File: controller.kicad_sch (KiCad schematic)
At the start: 23 parts, among them U4 STM32H742VGTx

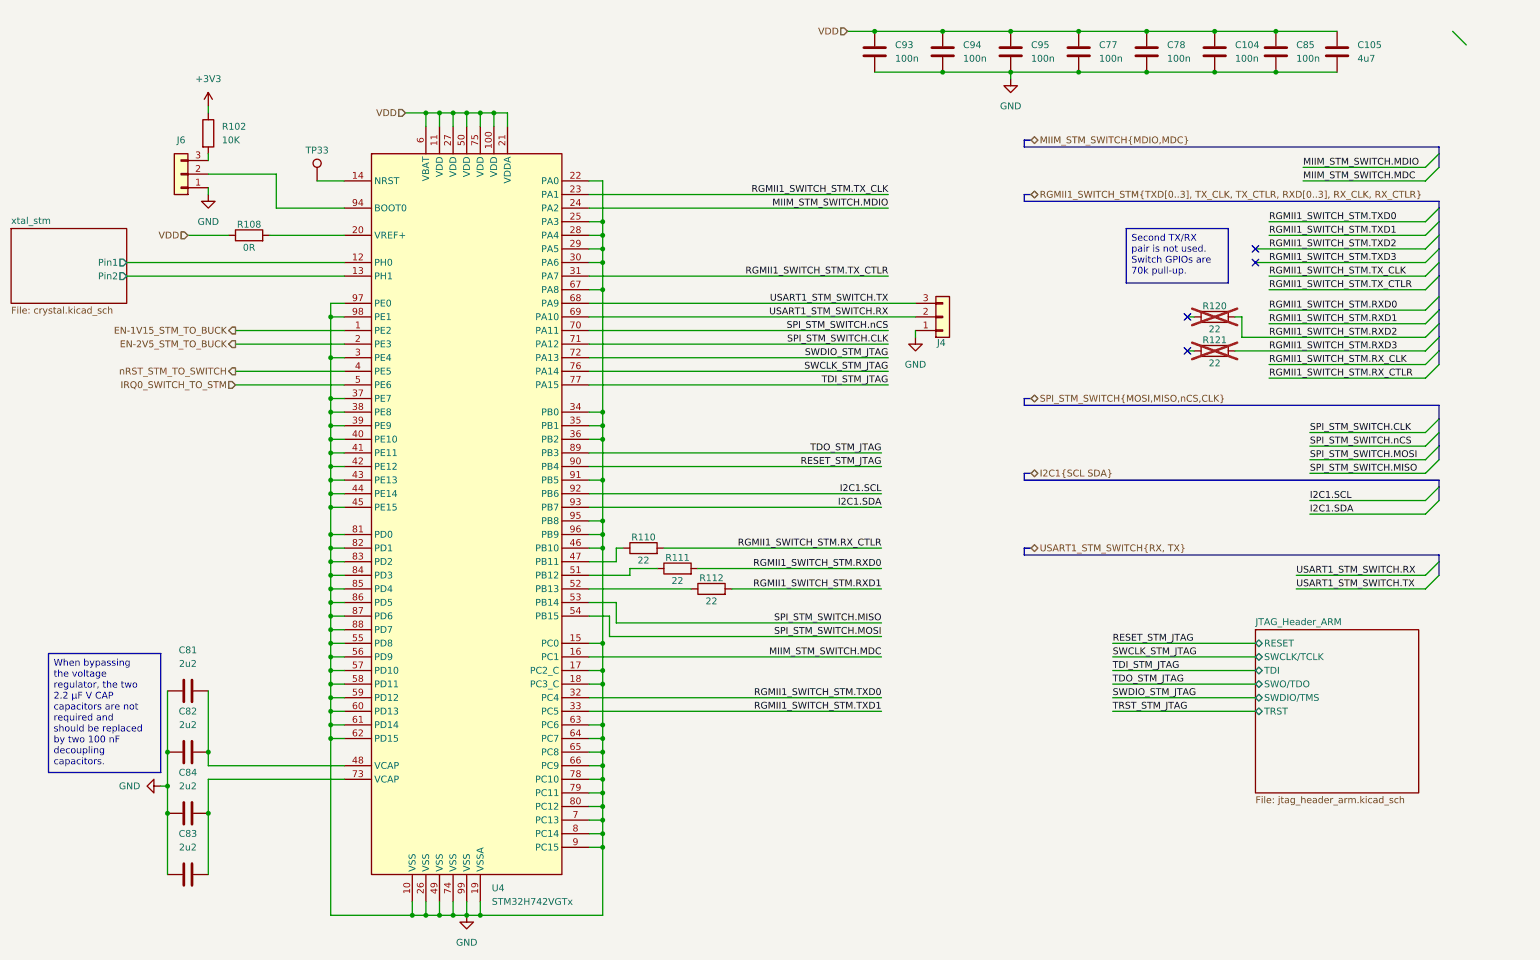
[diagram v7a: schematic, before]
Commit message: updates components from my library misconfiguration. Refs: #1
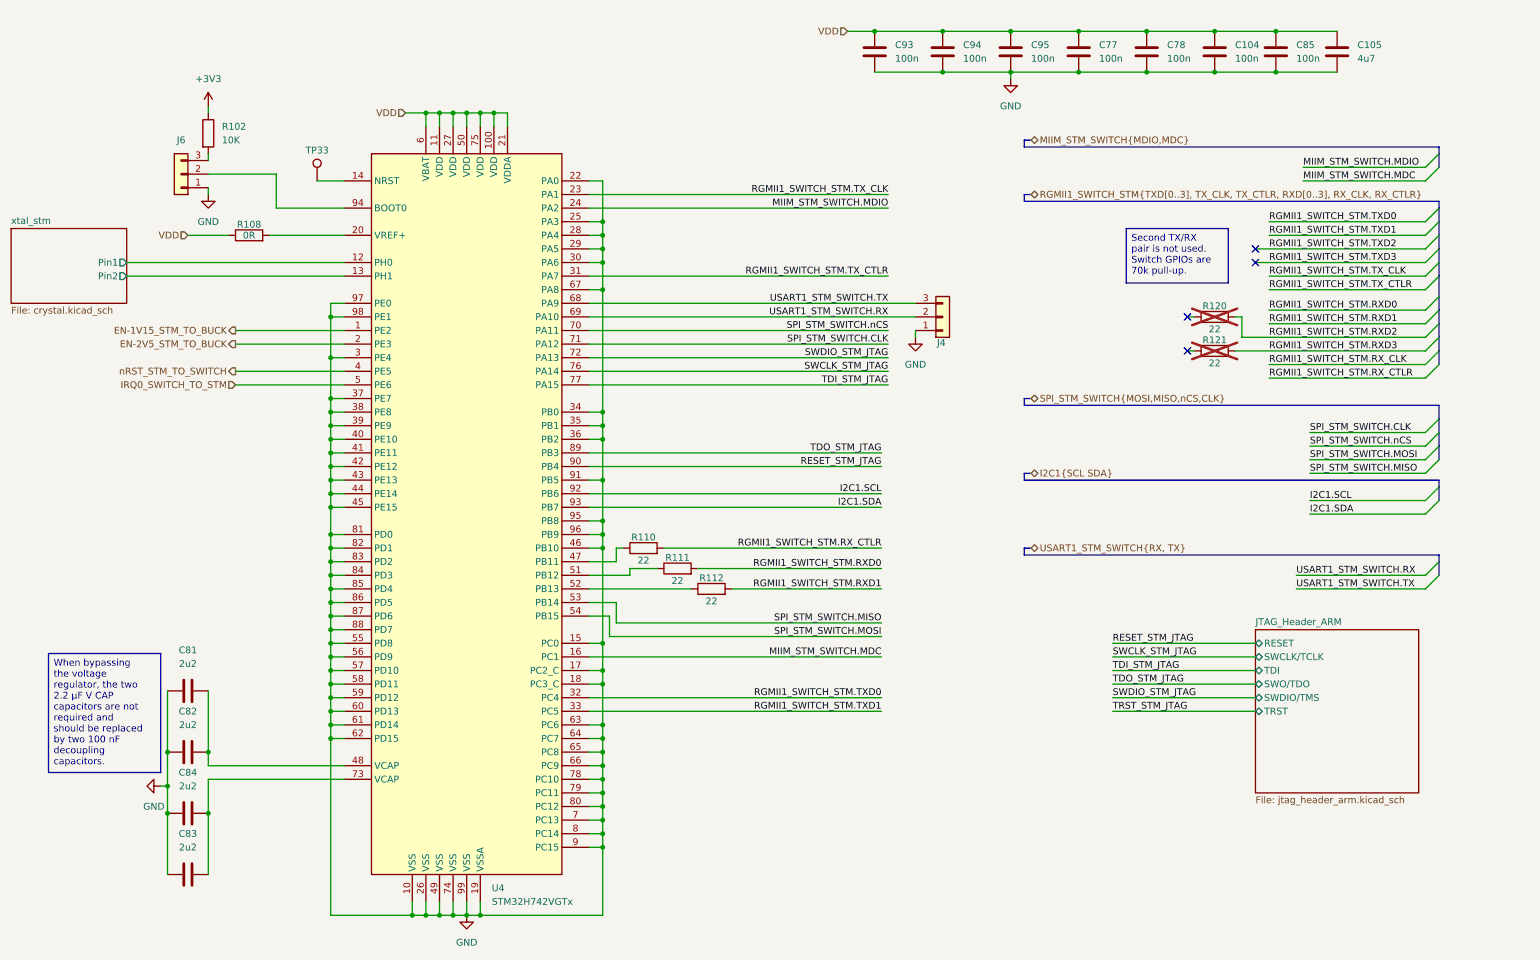
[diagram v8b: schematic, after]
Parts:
- C104, C77, C78, C85, C93, C94, C95: symbol KL_C:C_100n_10V_10_X7R_0603 -> KL_C:C_100n_10V_X7R_0603_10; Dielectric_type X7R -> (none); Digikey 311-4053-1-ND -> 311-4055-1-ND; LCSC C36911391 -> C519438; Mouser 603-CC603KRX7R6BB102 -> 603-CC603KRX7R6BB104; Voltage 10 -> 50
- C105: symbol KL_C:C_4u7_10V_10_X5R_0603 -> KL_C:C_4u7_10V_X5R_0603_10; Dielectric_type X5R -> (none)
- C81, C82, C83, C84: symbol KL_C:C_2u2_10V_20_Y5V_0603 -> KL_C:C_2u2_10V_Y5V_0603_20; Dielectric_type Y5V -> (none); Digikey 311-3413-1-ND -> (none); LCSC C3888308 -> (none); Mouser 603-CC603MRY5V6BB225 -> (none); Tolerance 20 -> (none); Voltage 10 -> (none)
- R108: Package (in) (none) -> 2512
- U4: footprint KL_Footprints:LQFP-100_14x14mm_P0.5mm -> Package_QFP:LQFP-100_14x14mm_P0.5mm
